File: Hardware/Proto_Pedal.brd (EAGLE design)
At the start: 85.1 x 110.5 mm, 124 parts, among them Q1 2.5A/30V

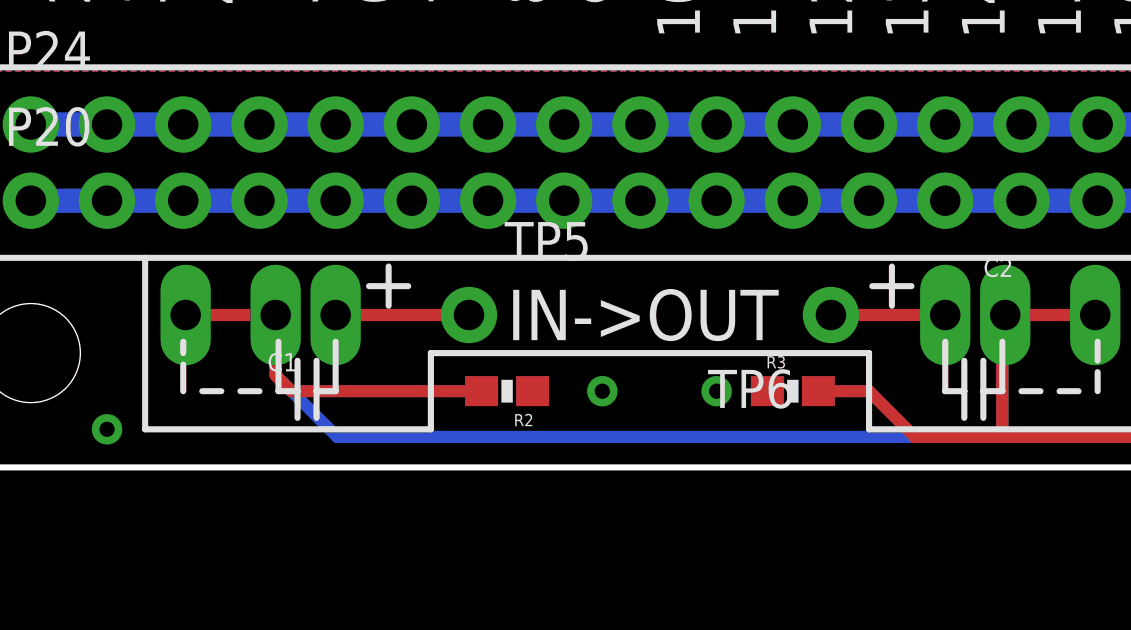
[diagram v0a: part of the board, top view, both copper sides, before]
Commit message: Fixing what Eric found in review.
-I/O coupling caps now have similar trace arrangements.
-Second page of Schem bumped to V10.
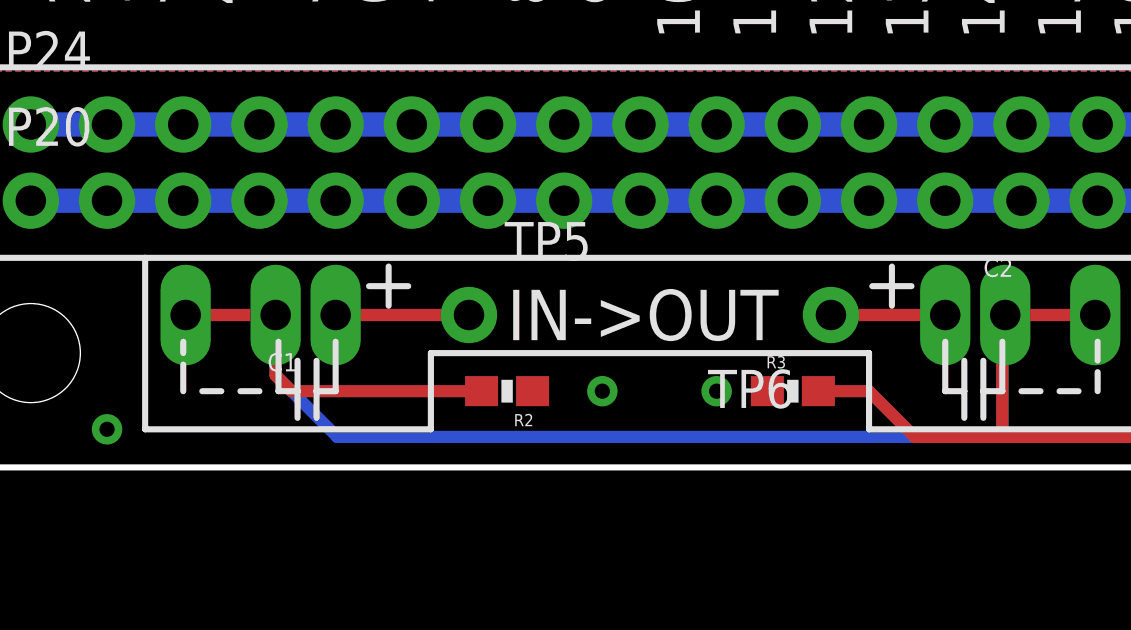
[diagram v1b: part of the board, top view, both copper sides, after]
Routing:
- net N$68: track 3.81 -> 7.62 mm
- net FX_IN: track 72.2 -> 75.2 mm
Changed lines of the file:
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@@
 <layer number="14" name="Route14" color="1" fill="6" visible="no" active="no"/>
 <layer number="15" name="Route15" color="4" fill="6" visible="no" active="no"/>
-<layer number="16" name="Bottom" color="1" fill="1" visible="yes" active="yes"/>
+<layer number="16" name="Bottom" color="1" fill="1" visible="no" active="yes"/>
 <layer number="17" name="Pads" color="2" fill="1" visible="yes" active="yes"/>
 <layer number="18" name="Vias" color="2" fill="1" visible="yes" active="yes"/>
@@
 <layer number="27" name="tValues" color="7" fill="1" visible="no" active="yes"/>
 <layer number="28" name="bValues" color="7" fill="1" visible="no" active="yes"/>
-<layer number="29" name="tStop" color="7" fill="3" visible="yes" active="yes"/>
-<layer number="30" name="bStop" color="7" fill="6" visible="yes" active="yes"/>
+<layer number="29" name="tStop" color="7" fill="3" visible="no" active="yes"/>
+<layer number="30" name="bStop" color="7" fill="6" visible="no" active="yes"/>
 <layer number="31" name="tCream" color="7" fill="4" visible="no" active="yes"/>
 <layer number="32" name="bCream" color="7" fill="5" visible="no" active="yes"/>
@@
 <layer number="37" name="tTest" color="7" fill="1" visible="no" active="yes"/>
 <layer number="38" name="bTest" color="7" fill="1" visible="no" active="yes"/>
-<layer number="39" name="tKeepout" color="4" fill="11" visible="yes" active="yes"/>
-<layer number="40" name="bKeepout" color="1" fill="11" visible="yes" active="yes"/>
+<layer number="39" name="tKeepout" color="4" fill="11" visible="no" active="yes"/>
+<layer number="40" name="bKeepout" color="1" fill="11" visible="no" active="yes"/>
 <layer number="41" name="tRestrict" color="4" fill="10" visible="no" active="yes"/>
 <layer number="42" name="bRestrict" color="1" fill="10" visible="no" active="yes"/>
@@
 <wire x1="11.97" y1="23.39" x2="11.97" y2="25.4" width="0.4064" layer="1"/>
 <wire x1="14.024" y1="21.336" x2="11.97" y2="23.39" width="0.4064" layer="16"/>
+<wire x1="11.97" y1="25.4" x2="8.985" y2="25.4" width="0.4064" layer="16"/>
 </signal>
 <signal name="FX_OUT">
@@
 <contactref element="C2" pad="P$1"/>
 <wire x1="30.48" y1="25.4" x2="34.29" y2="25.4" width="0.4064" layer="1"/>
+<wire x1="30.48" y1="25.4" x2="34.29" y2="25.4" width="0.4064" layer="16"/>
 </signal>
 </signals>
